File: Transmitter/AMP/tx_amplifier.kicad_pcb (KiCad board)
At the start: 2 copper layers, 30 x 30 mm, 20 parts, among them J1 Conn_Coaxial, J2 Conn_Coaxial, J3 Screw_Terminal_01x02, Q1 BFR740L3RH

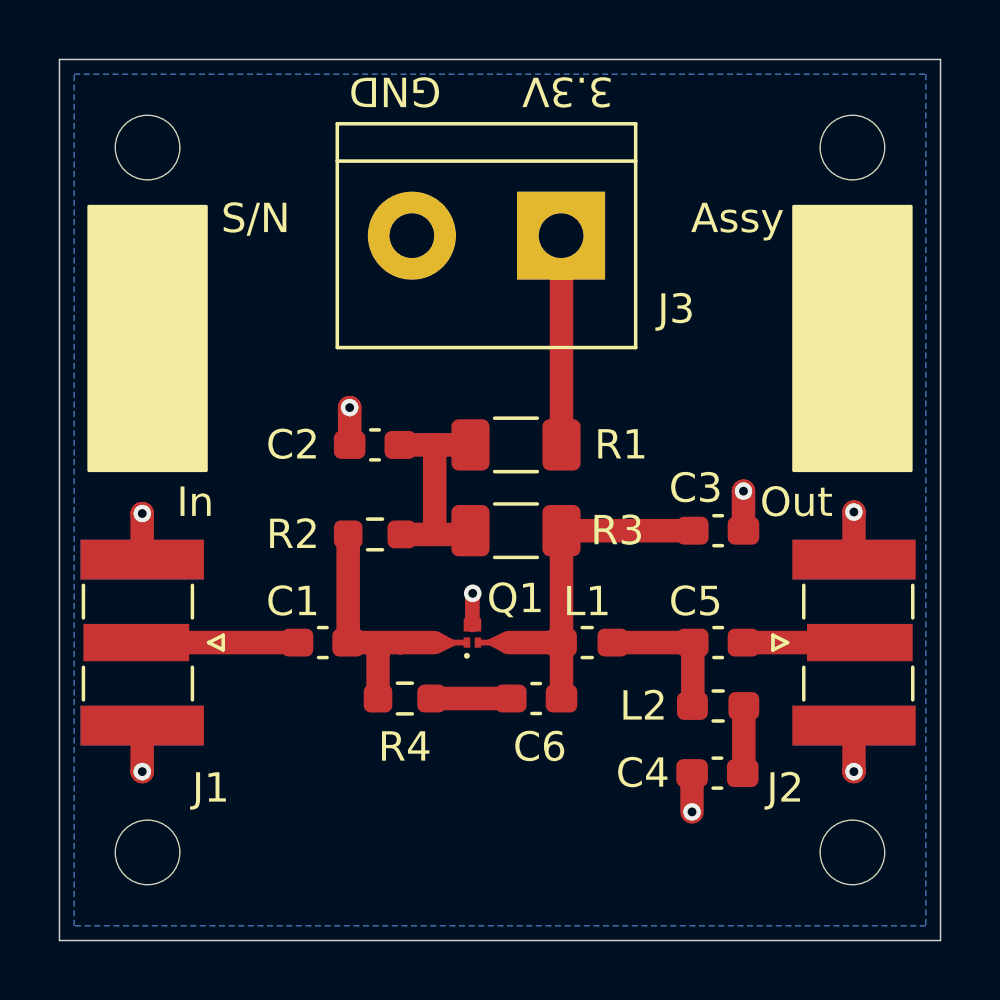
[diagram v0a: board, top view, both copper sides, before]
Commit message: tx amplifier v1.1
Change M2 to M3 screws
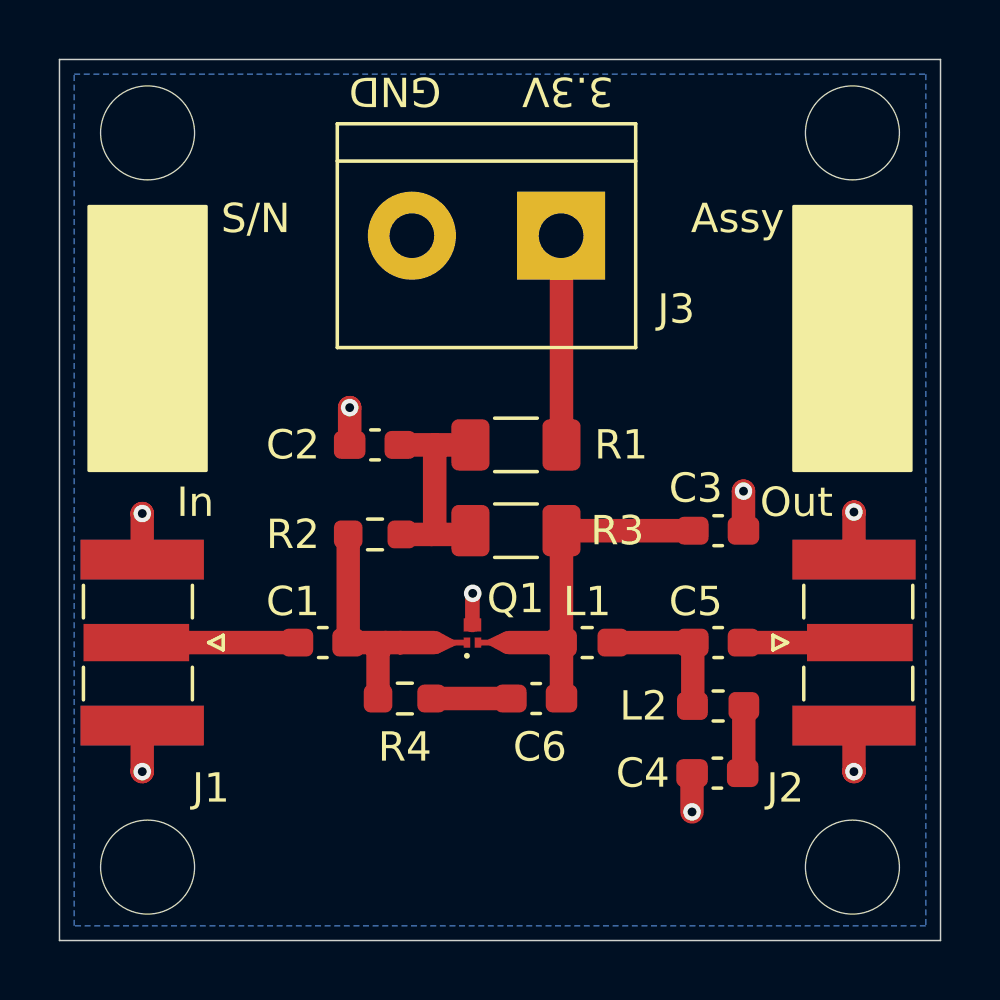
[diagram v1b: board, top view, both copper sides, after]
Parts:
- H1, H2, H3, H4: value M2 -> M3; footprint MountingHole:MountingHole_2.2mm_M2_ISO7380 -> MountingHole:MountingHole_3.2mm_M3_ISO7380
- moved H1 0.50 mm to (103.0, 92.5)
- moved H2 0.50 mm to (127.0, 92.5)
- moved H3 0.50 mm to (103.0, 117.5)
- moved H4 0.50 mm to (127.0, 117.5)
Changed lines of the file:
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@@
 		(title "Amplificador TX")
 		(date "2025-01-07")
-		(rev "v1.0")
+		(rev "v1.1")
 		(company "Cotti Nicolas Gabriel")
 		(comment 1 "ncotti@frba.utn.edu.ar")
@@
 		)
 	)
-	(footprint "MountingHole:MountingHole_2.2mm_M2_ISO7380"
+	(footprint "MountingHole:MountingHole_3.2mm_M3_ISO7380"
 		(layer "F.Cu")
-		(at 103 93)
-		(descr "Mounting Hole 2.2mm, no annular, M2, ISO7380")
-		(tags "mounting hole 2.2mm no annular m2 iso7380")
+		(at 103 92.5)
+		(descr "Mounting Hole 3.2mm, no annular, M3, ISO7380")
+		(tags "mounting hole 3.2mm no annular m3 iso7380")
 		(property "Reference" "H1"
-			(at 0 -2.75 0)
+			(at 0 -3.85 0)
 			(layer "F.SilkS")
 			(hide yes)
@@
 			)
 		)
-		(property "Value" "M2"
-			(at 0 2.75 0)
+		(property "Value" "M3"
+			(at 0 3.85 0)
 			(layer "F.Fab")
 			(effects
@@
 			)
 		)
-		(property "Footprint" "MountingHole:MountingHole_2.2mm_M2_ISO7380"
+		(property "Footprint" "MountingHole:MountingHole_3.2mm_M3_ISO7380"
 			(at 0 0 0)
 			(layer "F.Fab")
@@
 		(fp_circle
 			(center 0 0)
-			(end 1.75 0)
+			(end 2.85 0)
 			(stroke
 				(width 0.15)
@@
 		(fp_circle
 			(center 0 0)
-			(end 2 0)
+			(end 3.1 0)
 			(stroke
 				(width 0.05)
@@
 		(pad "" np_thru_hole circle
 			(at 0 0)
-			(size 2.2 2.2)
-			(drill 2.2)
+			(size 3.2 3.2)
+			(drill 3.2)
 			(layers "*.Cu" "*.Mask")
 		)
@@
 		)
 	)
-	(footprint "MountingHole:MountingHole_2.2mm_M2_ISO7380"
+	(footprint "MountingHole:MountingHole_3.2mm_M3_ISO7380"
 		(layer "F.Cu")
-		(at 127 93)
-		(descr "Mounting Hole 2.2mm, no annular, M2, ISO7380")
-		(tags "mounting hole 2.2mm no annular m2 iso7380")
+		(at 127 92.5)
+		(descr "Mounting Hole 3.2mm, no annular, M3, ISO7380")
+		(tags "mounting hole 3.2mm no annular m3 iso7380")
 		(property "Reference" "H2"
-			(at 0 -2.75 0)
+			(at 0 -3.85 0)
 			(layer "F.SilkS")
 			(hide yes)
@@
 			)
 		)
-		(property "Value" "M2"
-			(at 0 2.75 0)
+		(property "Value" "M3"
+			(at 0 3.85 0)
 			(layer "F.Fab")
 			(effects
@@
 			)
 		)
-		(property "Footprint" "MountingHole:MountingHole_2.2mm_M2_ISO7380"
+		(property "Footprint" "MountingHole:MountingHole_3.2mm_M3_ISO7380"
 			(at 0 0 0)
 			(layer "F.Fab")
@@
 		(fp_circle
 			(center 0 0)
-			(end 1.75 0)
+			(end 2.85 0)
 			(stroke
 				(width 0.15)
@@
 		(fp_circle
 			(center 0 0)
-			(end 2 0)
+			(end 3.1 0)
 			(stroke
 				(width 0.05)
@@
 		(pad "" np_thru_hole circle
 			(at 0 0)
-			(size 2.2 2.2)
-			(drill 2.2)
+			(size 3.2 3.2)
+			(drill 3.2)
 			(layers "*.Cu" "*.Mask")
 		)
@@
 		)
 	)
-	(footprint "MountingHole:MountingHole_2.2mm_M2_ISO7380"
+	(footprint "MountingHole:MountingHole_3.2mm_M3_ISO7380"
 		(layer "F.Cu")
-		(at 127 117)
-		(descr "Mounting Hole 2.2mm, no annular, M2, ISO7380")
-		(tags "mounting hole 2.2mm no annular m2 iso7380")
+		(at 127 117.5)
+		(descr "Mounting Hole 3.2mm, no annular, M3, ISO7380")
+		(tags "mounting hole 3.2mm no annular m3 iso7380")
 		(property "Reference" "H4"
-			(at 0 -2.75 0)
+			(at 0 -3.85 0)
 			(layer "F.SilkS")
 			(hide yes)
@@
 			)
 		)
-		(property "Value" "M2"
-			(at 0 2.75 0)
+		(property "Value" "M3"
+			(at 0 3.85 0)
 			(layer "F.Fab")
 			(effects
@@
 			)
 		)
-		(property "Footprint" "MountingHole:MountingHole_2.2mm_M2_ISO7380"
+		(property "Footprint" "MountingHole:MountingHole_3.2mm_M3_ISO7380"
 			(at 0 0 0)
 			(layer "F.Fab")
@@
 		(fp_circle
 			(center 0 0)
-			(end 1.75 0)
+			(end 2.85 0)
 			(stroke
 				(width 0.15)
@@
 		(fp_circle
 			(center 0 0)
-			(end 2 0)
+			(end 3.1 0)
 			(stroke
 				(width 0.05)
@@
 		(pad "" np_thru_hole circle
 			(at 0 0)
-			(size 2.2 2.2)
-			(drill 2.2)
+			(size 3.2 3.2)
+			(drill 3.2)
 			(layers "*.Cu" "*.Mask")
 		)
 	)
-	(footprint "MountingHole:MountingHole_2.2mm_M2_ISO7380"
+	(footprint "MountingHole:MountingHole_3.2mm_M3_ISO7380"
 		(layer "F.Cu")
-		(at 103 117)
-		(descr "Mounting Hole 2.2mm, no annular, M2, ISO7380")
-		(tags "mounting hole 2.2mm no annular m2 iso7380")
+		(at 103 117.5)
+		(descr "Mounting Hole 3.2mm, no annular, M3, ISO7380")
+		(tags "mounting hole 3.2mm no annular m3 iso7380")
 		(property "Reference" "H3"
-			(at 0 -2.75 0)
+			(at 0 -3.85 0)
 			(layer "F.SilkS")
 			(hide yes)
@@
 			)
 		)
-		(property "Value" "M2"
-			(at 0 2.75 0)
+		(property "Value" "M3"
+			(at 0 3.85 0)
 			(layer "F.Fab")
 			(effects
@@
 			)
 		)
-		(property "Footprint" "MountingHole:MountingHole_2.2mm_M2_ISO7380"
+		(property "Footprint" "MountingHole:MountingHole_3.2mm_M3_ISO7380"
 			(at 0 0 0)
 			(layer "F.Fab")
@@
 		(fp_circle
 			(center 0 0)
-			(end 1.75 0)
+			(end 2.85 0)
 			(stroke
 				(width 0.15)
@@
 		(fp_circle
 			(center 0 0)
-			(end 2 0)
+			(end 3.1 0)
 			(stroke
 				(width 0.05)
@@
 		(pad "" np_thru_hole circle
 			(at 0 0)
-			(size 2.2 2.2)
-			(drill 2.2)
+			(size 3.2 3.2)
+			(drill 3.2)
 			(layers "*.Cu" "*.Mask")
 		)
@@
 			(font
 				(size 1 1)
-				(thickness 0.1)
+				(thickness 0.15)
 			)
 			(justify left bottom)
@@
 			(font
 				(size 1 1)
-				(thickness 0.1)
+				(thickness 0.15)
 			)
 			(justify left bottom)
@@
 			(font
 				(size 1 1)
-				(thickness 0.1)
+				(thickness 0.15)
 			)
 			(justify left bottom)
@@
 			(font
 				(size 1 1)
-				(thickness 0.1)
+				(thickness 0.15)
 			)
 			(justify left bottom)
@@
 	)
 	(segment
-		(start 113.8741 109.855)
-		(end 113.2488 109.855)
-		(width 0.2)
-		(layer "F.Cu")
-		(net 1)
-	)
-	(segment
 		(start 110.8475 110.1065)
 		(end 111.099 109.855)
@@
 	)
 	(segment
+		(start 113.8741 109.855)
+		(end 112.75 109.855)
+		(width 0.2)
+		(layer "F.Cu")
+		(net 1)
+	)
+	(segment
 		(start 111.099 109.855)
 		(end 109.829 109.855)
@@
 	)
 	(segment
-		(start 114.2486 109.855)
-		(end 114.9506 109.855)
-		(width 0.2)
-		(layer "F.Cu")
-		(net 5)
-	)
-	(segment
 		(start 117.094 106.045)
 		(end 121.5655 106.045)
@@
 		(layer "F.Cu")
 		(net 5)
+	)
+	(segment
+		(start 114.2486 109.855)
+		(end 115.3154 109.855)
+		(width 0.2)
+		(layer "F.Cu")
+		(net 5)

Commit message: Add CPW to preenfasis and tx amplifier
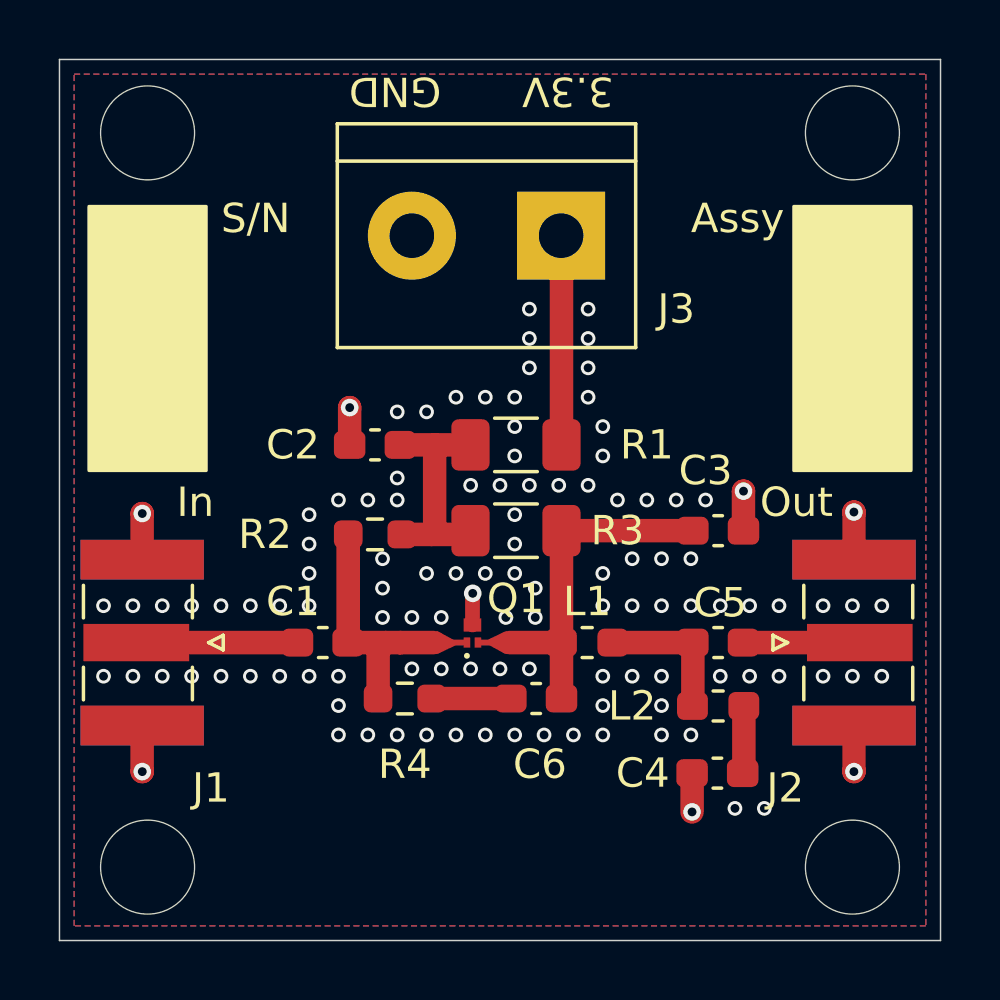
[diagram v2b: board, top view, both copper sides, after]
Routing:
- net GND: vias 8 -> 116
- added copper zone on F.Cu, net GND

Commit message: Modified some thermal reliefs
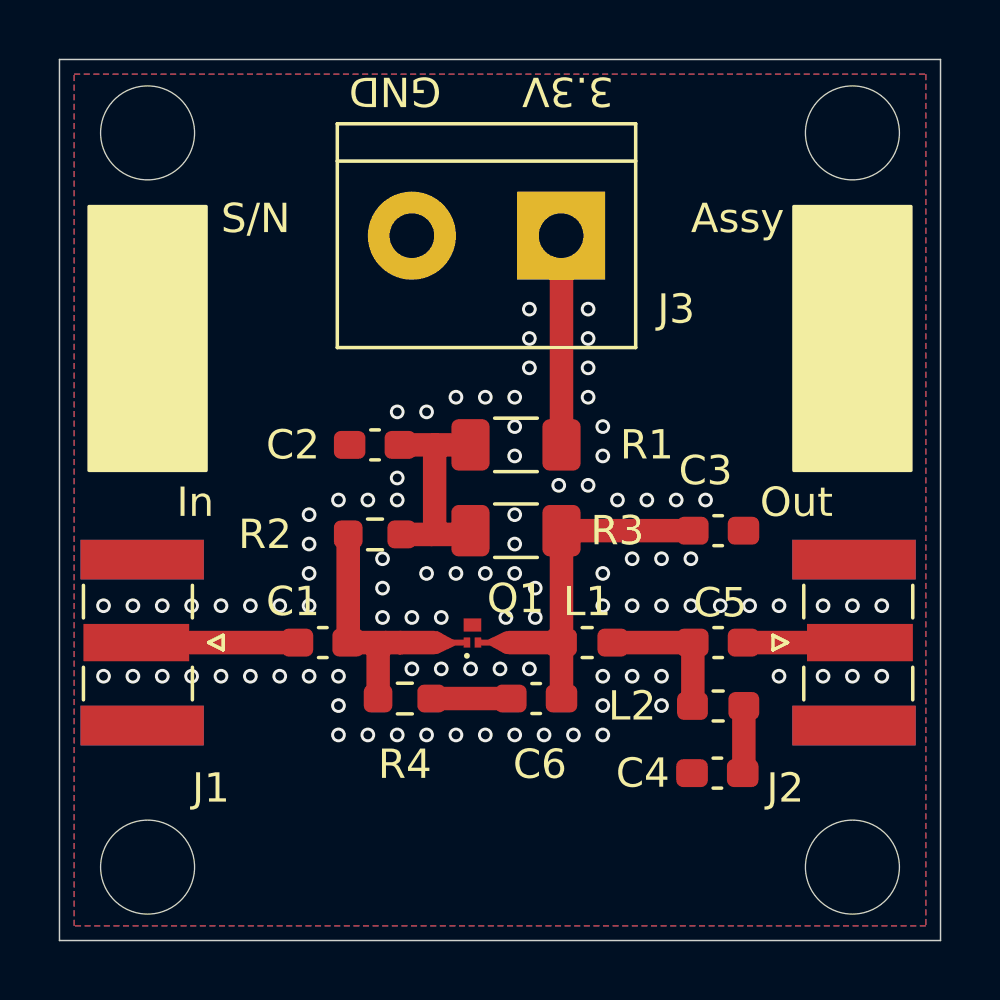
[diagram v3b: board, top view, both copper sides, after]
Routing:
- net GND: track 11.4 -> 0.00 mm, vias 116 -> 99
